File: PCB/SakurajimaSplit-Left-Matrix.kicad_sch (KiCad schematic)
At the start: 42 parts

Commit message: feat(pcb): assign all footprints
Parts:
- D10: renamed from D32; footprint (none) -> Diode_SMD:D_SOD-123
- D11: renamed from D33; footprint (none) -> Diode_SMD:D_SOD-123
- D12: renamed from D34; footprint (none) -> Diode_SMD:D_SOD-123
- D13: renamed from D35; footprint (none) -> Diode_SMD:D_SOD-123
- D14: renamed from D36; footprint (none) -> Diode_SMD:D_SOD-123
- D15: renamed from D37; footprint (none) -> Diode_SMD:D_SOD-123
- D16: renamed from D38; footprint (none) -> Diode_SMD:D_SOD-123
- D17: renamed from D39; footprint (none) -> Diode_SMD:D_SOD-123
- D18: renamed from D40; footprint (none) -> Diode_SMD:D_SOD-123
- D19: renamed from D41; footprint (none) -> Diode_SMD:D_SOD-123
- D20: renamed from D42; footprint (none) -> Diode_SMD:D_SOD-123
- D21: renamed from D43; footprint (none) -> Diode_SMD:D_SOD-123
- D22: renamed from D44; footprint (none) -> Diode_SMD:D_SOD-123
- D23: renamed from D45; footprint (none) -> Diode_SMD:D_SOD-123
- D24: renamed from D46; footprint (none) -> Diode_SMD:D_SOD-123
- D4: renamed from D26; footprint (none) -> Diode_SMD:D_SOD-123
- D5: renamed from D27; footprint (none) -> Diode_SMD:D_SOD-123
- D6: renamed from D28; footprint (none) -> Diode_SMD:D_SOD-123
- D7: renamed from D29; footprint (none) -> Diode_SMD:D_SOD-123
- D8: renamed from D30; footprint (none) -> Diode_SMD:D_SOD-123
- D9: renamed from D31; footprint (none) -> Diode_SMD:D_SOD-123
- MX1: renamed from MX22; footprint (none) -> PCM_marbastlib-mx:SW_MX_1u
- MX10: renamed from MX31; footprint (none) -> PCM_marbastlib-mx:SW_MX_1u
- MX11: renamed from MX32; footprint (none) -> PCM_marbastlib-mx:SW_MX_1u
- MX12: renamed from MX33; footprint (none) -> PCM_marbastlib-mx:SW_MX_1u
- MX13: renamed from MX34; footprint (none) -> PCM_marbastlib-mx:SW_MX_1u
- MX14: renamed from MX35; footprint (none) -> PCM_marbastlib-mx:SW_MX_1u
- MX15: renamed from MX36; footprint (none) -> PCM_marbastlib-mx:SW_MX_1u
- MX16: renamed from MX37; footprint (none) -> PCM_marbastlib-mx:SW_MX_1u
- MX17: renamed from MX38; footprint (none) -> PCM_marbastlib-mx:SW_MX_1u
- MX18: renamed from MX39; footprint (none) -> PCM_marbastlib-mx:SW_MX_1u
- MX19: renamed from MX40; footprint (none) -> PCM_marbastlib-mx:SW_MX_1u
- MX2: renamed from MX23; footprint (none) -> PCM_marbastlib-mx:SW_MX_1u
- MX20: renamed from MX41; footprint (none) -> PCM_marbastlib-mx:SW_MX_1u
- MX21: renamed from MX42; footprint (none) -> PCM_marbastlib-mx:SW_MX_1u
- MX3: renamed from MX24; footprint (none) -> PCM_marbastlib-mx:SW_MX_1u
- MX4: renamed from MX25; footprint (none) -> PCM_marbastlib-mx:SW_MX_1u
- MX5: renamed from MX26; footprint (none) -> PCM_marbastlib-mx:SW_MX_1u
- MX6: renamed from MX27; footprint (none) -> PCM_marbastlib-mx:SW_MX_1u
- MX7: renamed from MX28; footprint (none) -> PCM_marbastlib-mx:SW_MX_1u
- MX8: renamed from MX29; footprint (none) -> PCM_marbastlib-mx:SW_MX_1u
- MX9: renamed from MX30; footprint (none) -> PCM_marbastlib-mx:SW_MX_1u

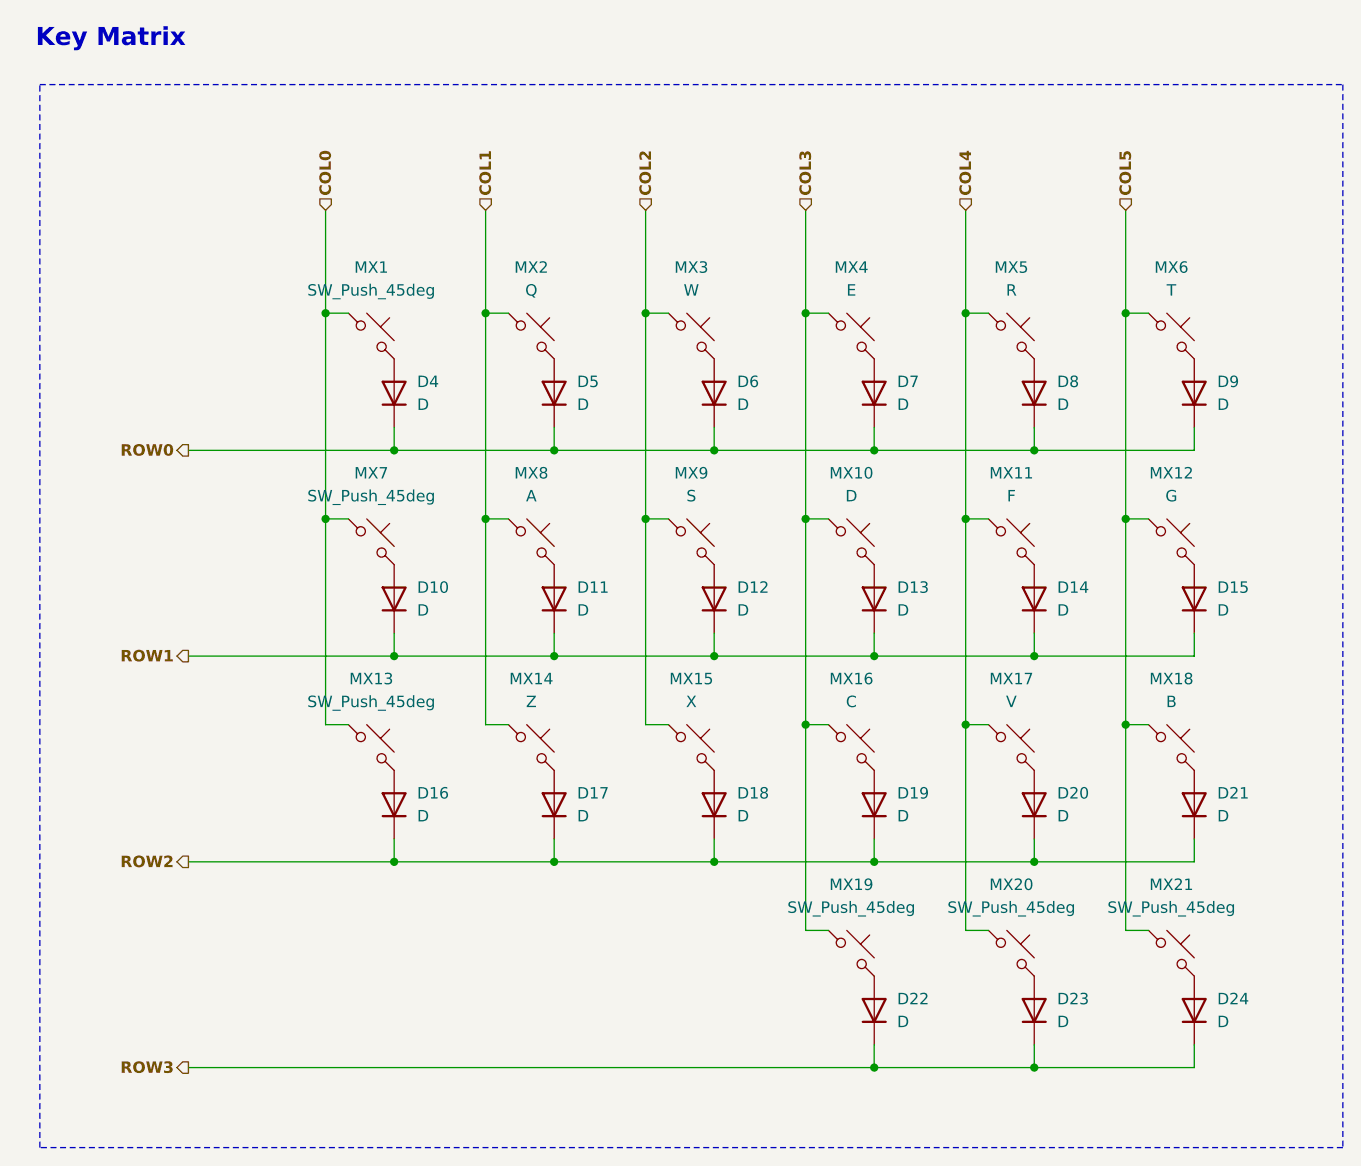
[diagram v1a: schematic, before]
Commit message: fix(sch): fix matrix diode designators not starting from 1
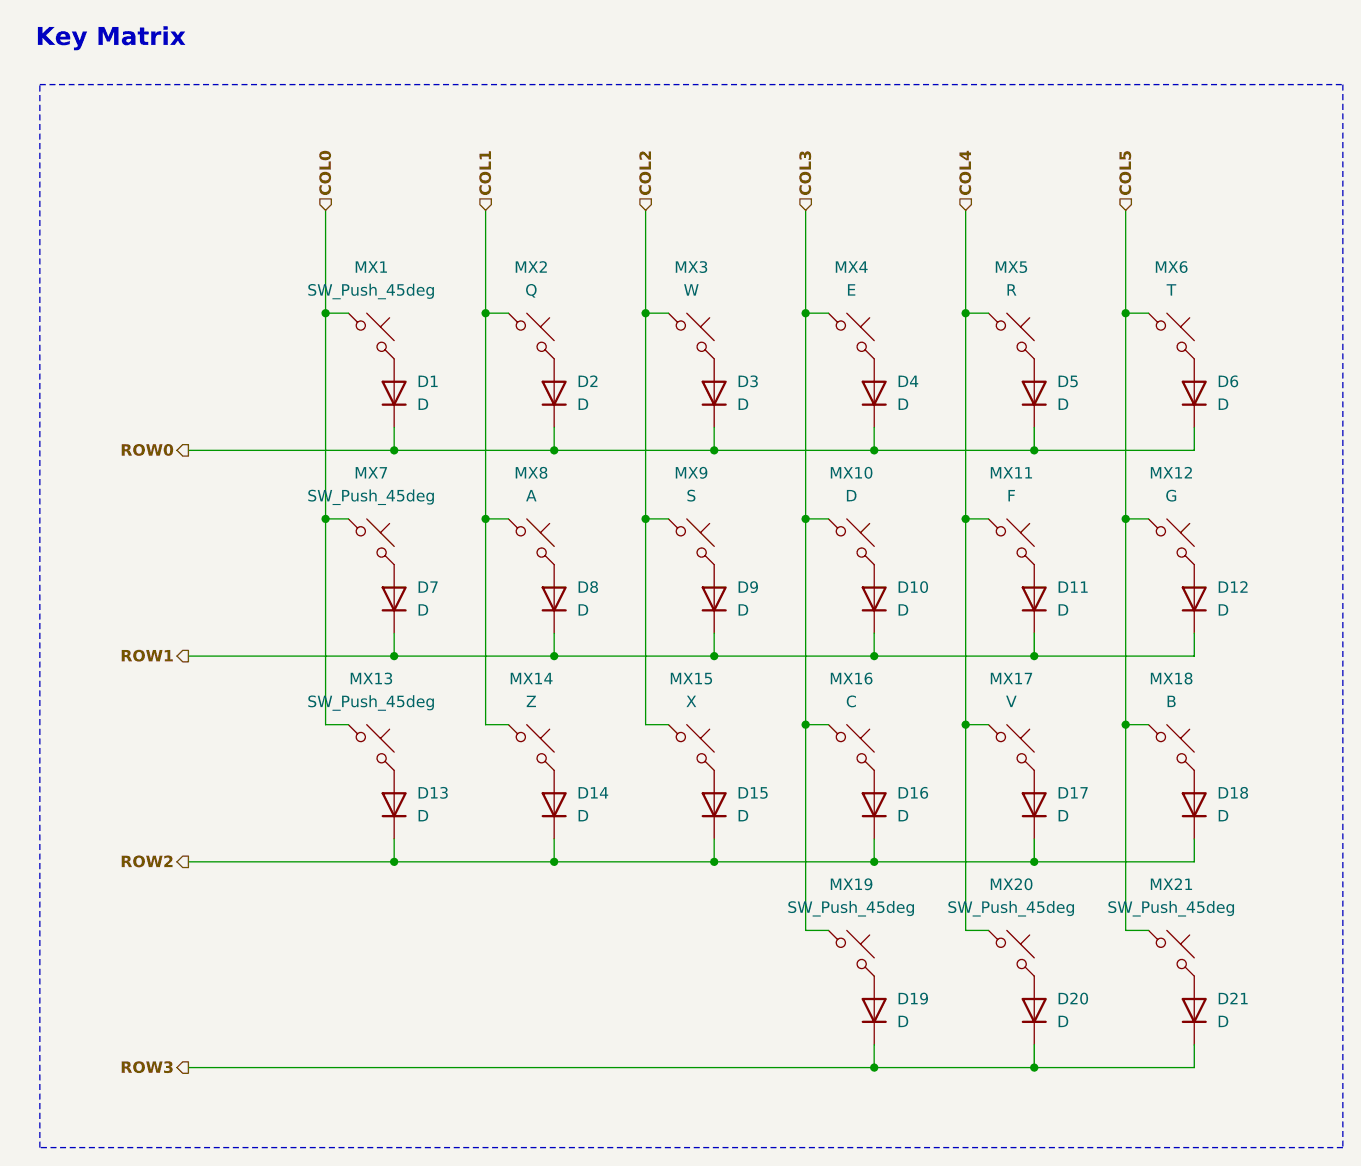
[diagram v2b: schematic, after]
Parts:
- renumbered D4 to D1, D13 to D10, D14 to D11, D15 to D12, D16 to D13, D17 to D14, D18 to D15, D19 to D16, D20 to D17, D21 to D18, D22 to D19, D5 to D2, D23 to D20, D24 to D21, D6 to D3, D7 to D4, D8 to D5, D9 to D6, D10 to D7, D11 to D8, D12 to D9
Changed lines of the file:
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@@
 		(dnp no)
 		(fields_autoplaced yes)
-		(property "Reference" "D21"
+		(property "Reference" "D18"
 			(at 267.97 158.7499 90)
 			(effects
@@
 			(project "SakurajimaSplit"
 				(path "/2049b6de-7453-46e1-ab60-70116abff9d6/d08add9a-e5d5-49be-809e-a90adb11436d/aea2268b-99a7-4c1b-88ca-9db0e6f54310"
-					(reference "D21")
+					(reference "D18")
 					(unit 1)
 				)
@@
 		(dnp no)
 		(fields_autoplaced yes)
-		(property "Reference" "D14"
+		(property "Reference" "D11"
 			(at 250.19 135.8899 90)
 			(effects
@@
 			(project "SakurajimaSplit"
 				(path "/2049b6de-7453-46e1-ab60-70116abff9d6/d08add9a-e5d5-49be-809e-a90adb11436d/aea2268b-99a7-4c1b-88ca-9db0e6f54310"
-					(reference "D14")
+					(reference "D11")
 					(unit 1)
 				)
@@
 		(dnp no)
 		(fields_autoplaced yes)
-		(property "Reference" "D9"
+		(property "Reference" "D6"
 			(at 267.97 113.0299 90)
 			(effects
@@
 			(project "SakurajimaSplit"
 				(path "/2049b6de-7453-46e1-ab60-70116abff9d6/d08add9a-e5d5-49be-809e-a90adb11436d/aea2268b-99a7-4c1b-88ca-9db0e6f54310"
-					(reference "D9")
+					(reference "D6")
 					(unit 1)
 				)
@@
 		(dnp no)
 		(fields_autoplaced yes)
-		(property "Reference" "D5"
+		(property "Reference" "D2"
 			(at 196.85 113.0299 90)
 			(effects
@@
 			(project "SakurajimaSplit"
 				(path "/2049b6de-7453-46e1-ab60-70116abff9d6/d08add9a-e5d5-49be-809e-a90adb11436d/aea2268b-99a7-4c1b-88ca-9db0e6f54310"
-					(reference "D5")
+					(reference "D2")
 					(unit 1)
 				)
@@
 		(dnp no)
 		(fields_autoplaced yes)
-		(property "Reference" "D12"
+		(property "Reference" "D9"
 			(at 214.63 135.8899 90)
 			(effects
@@
 			(project "SakurajimaSplit"
 				(path "/2049b6de-7453-46e1-ab60-70116abff9d6/d08add9a-e5d5-49be-809e-a90adb11436d/aea2268b-99a7-4c1b-88ca-9db0e6f54310"
-					(reference "D12")
+					(reference "D9")
 					(unit 1)
 				)
@@
 		(dnp no)
 		(fields_autoplaced yes)
-		(property "Reference" "D13"
+		(property "Reference" "D10"
 			(at 232.41 135.8899 90)
 			(effects
@@
 			(project "SakurajimaSplit"
 				(path "/2049b6de-7453-46e1-ab60-70116abff9d6/d08add9a-e5d5-49be-809e-a90adb11436d/aea2268b-99a7-4c1b-88ca-9db0e6f54310"
-					(reference "D13")
+					(reference "D10")
 					(unit 1)
 				)
@@
 		(dnp no)
 		(fields_autoplaced yes)
-		(property "Reference" "D24"
+		(property "Reference" "D21"
 			(at 267.97 181.6099 90)
 			(effects
@@
 			(project "SakurajimaSplit"
 				(path "/2049b6de-7453-46e1-ab60-70116abff9d6/d08add9a-e5d5-49be-809e-a90adb11436d/aea2268b-99a7-4c1b-88ca-9db0e6f54310"
-					(reference "D24")
+					(reference "D21")
 					(unit 1)
 				)
@@
 		(dnp no)
 		(fields_autoplaced yes)
-		(property "Reference" "D6"
+		(property "Reference" "D3"
 			(at 214.63 113.0299 90)
 			(effects
@@
 			(project "SakurajimaSplit"
 				(path "/2049b6de-7453-46e1-ab60-70116abff9d6/d08add9a-e5d5-49be-809e-a90adb11436d/aea2268b-99a7-4c1b-88ca-9db0e6f54310"
-					(reference "D6")
+					(reference "D3")
 					(unit 1)
 				)
@@
 		(dnp no)
 		(fields_autoplaced yes)
-		(property "Reference" "D18"
+		(property "Reference" "D15"
 			(at 214.63 158.7499 90)
 			(effects
@@
 			(project "SakurajimaSplit"
 				(path "/2049b6de-7453-46e1-ab60-70116abff9d6/d08add9a-e5d5-49be-809e-a90adb11436d/aea2268b-99a7-4c1b-88ca-9db0e6f54310"
-					(reference "D18")
+					(reference "D15")
 					(unit 1)
 				)
@@
 		(dnp no)
 		(fields_autoplaced yes)
-		(property "Reference" "D16"
+		(property "Reference" "D13"
 			(at 179.07 158.7499 90)
 			(effects
@@
 			(project "SakurajimaSplit"
 				(path "/2049b6de-7453-46e1-ab60-70116abff9d6/d08add9a-e5d5-49be-809e-a90adb11436d/aea2268b-99a7-4c1b-88ca-9db0e6f54310"
-					(reference "D16")
+					(reference "D13")
 					(unit 1)
 				)
@@
 		(dnp no)
 		(fields_autoplaced yes)
-		(property "Reference" "D10"
+		(property "Reference" "D7"
 			(at 179.07 135.8899 90)
 			(effects
@@
 			(project "SakurajimaSplit"
 				(path "/2049b6de-7453-46e1-ab60-70116abff9d6/d08add9a-e5d5-49be-809e-a90adb11436d/aea2268b-99a7-4c1b-88ca-9db0e6f54310"
-					(reference "D10")
+					(reference "D7")
 					(unit 1)
 				)
@@
 		(dnp no)
 		(fields_autoplaced yes)
-		(property "Reference" "D11"
+		(property "Reference" "D8"
 			(at 196.85 135.8899 90)
 			(effects
@@
 			(project "SakurajimaSplit"
 				(path "/2049b6de-7453-46e1-ab60-70116abff9d6/d08add9a-e5d5-49be-809e-a90adb11436d/aea2268b-99a7-4c1b-88ca-9db0e6f54310"
-					(reference "D11")
+					(reference "D8")
 					(unit 1)
 				)
@@
 		(dnp no)
 		(fields_autoplaced yes)
-		(property "Reference" "D15"
+		(property "Reference" "D12"
 			(at 267.97 135.8899 90)
 			(effects
@@
 			(project "SakurajimaSplit"
 				(path "/2049b6de-7453-46e1-ab60-70116abff9d6/d08add9a-e5d5-49be-809e-a90adb11436d/aea2268b-99a7-4c1b-88ca-9db0e6f54310"
-					(reference "D15")
+					(reference "D12")
 					(unit 1)
 				)
@@
 		(dnp no)
 		(fields_autoplaced yes)
-		(property "Reference" "D17"
+		(property "Reference" "D14"
 			(at 196.85 158.7499 90)
 			(effects
@@
 			(project "SakurajimaSplit"
 				(path "/2049b6de-7453-46e1-ab60-70116abff9d6/d08add9a-e5d5-49be-809e-a90adb11436d/aea2268b-99a7-4c1b-88ca-9db0e6f54310"
-					(reference "D17")
+					(reference "D14")
 					(unit 1)
 				)
@@
 		(dnp no)
 		(fields_autoplaced yes)
-		(property "Reference" "D19"
+		(property "Reference" "D16"
 			(at 232.41 158.7499 90)
 			(effects
@@
 			(project "SakurajimaSplit"
 				(path "/2049b6de-7453-46e1-ab60-70116abff9d6/d08add9a-e5d5-49be-809e-a90adb11436d/aea2268b-99a7-4c1b-88ca-9db0e6f54310"
-					(reference "D19")
+					(reference "D16")
 					(unit 1)
 				)
@@
 		(dnp no)
 		(fields_autoplaced yes)
-		(property "Reference" "D7"
+		(property "Reference" "D4"
 			(at 232.41 113.0299 90)
 			(effects
@@
 			(project "SakurajimaSplit"
 				(path "/2049b6de-7453-46e1-ab60-70116abff9d6/d08add9a-e5d5-49be-809e-a90adb11436d/aea2268b-99a7-4c1b-88ca-9db0e6f54310"
-					(reference "D7")
+					(reference "D4")
 					(unit 1)
 				)
@@
 		(dnp no)
 		(fields_autoplaced yes)
-		(property "Reference" "D22"
+		(property "Reference" "D19"
 			(at 232.41 181.6099 90)
 			(effects
@@
 			(project "SakurajimaSplit"
 				(path "/2049b6de-7453-46e1-ab60-70116abff9d6/d08add9a-e5d5-49be-809e-a90adb11436d/aea2268b-99a7-4c1b-88ca-9db0e6f54310"
-					(reference "D22")
+					(reference "D19")
 					(unit 1)
 				)
@@
 		(dnp no)
 		(fields_autoplaced yes)
-		(property "Reference" "D23"
+		(property "Reference" "D20"
 			(at 250.19 181.6099 90)
 			(effects
@@
 			(project "SakurajimaSplit"
 				(path "/2049b6de-7453-46e1-ab60-70116abff9d6/d08add9a-e5d5-49be-809e-a90adb11436d/aea2268b-99a7-4c1b-88ca-9db0e6f54310"
-					(reference "D23")
+					(reference "D20")
 					(unit 1)
 				)
@@
 		(dnp no)
 		(fields_autoplaced yes)
-		(property "Reference" "D20"
+		(property "Reference" "D17"
 			(at 250.19 158.7499 90)
 			(effects
@@
 			(project "SakurajimaSplit"
 				(path "/2049b6de-7453-46e1-ab60-70116abff9d6/d08add9a-e5d5-49be-809e-a90adb11436d/aea2268b-99a7-4c1b-88ca-9db0e6f54310"
-					(reference "D20")
+					(reference "D17")
 					(unit 1)
 				)
@@
 		(dnp no)
 		(fields_autoplaced yes)
-		(property "Reference" "D8"
+		(property "Reference" "D5"
 			(at 250.19 113.0299 90)
 			(effects
@@
 			(project "SakurajimaSplit"
 				(path "/2049b6de-7453-46e1-ab60-70116abff9d6/d08add9a-e5d5-49be-809e-a90adb11436d/aea2268b-99a7-4c1b-88ca-9db0e6f54310"
-					(reference "D8")
+					(reference "D5")
 					(unit 1)
 				)
@@
 		(dnp no)
 		(fields_autoplaced yes)
-		(property "Reference" "D4"
+		(property "Reference" "D1"
 			(at 179.07 113.0299 90)
 			(effects
@@
 			(project "SakurajimaSplit"
 				(path "/2049b6de-7453-46e1-ab60-70116abff9d6/d08add9a-e5d5-49be-809e-a90adb11436d/aea2268b-99a7-4c1b-88ca-9db0e6f54310"
-					(reference "D4")
+					(reference "D1")
 					(unit 1)
 				)

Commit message: fix(sch): fix wrong footprint for MX21 & MX40
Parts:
- MX21: footprint PCM_marbastlib-mx:SW_MX_1u -> PCM_marbastlib-mx:SW_MX_1.5u
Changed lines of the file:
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@@
 			)
 		)
-		(property "Footprint" "PCM_marbastlib-mx:SW_MX_1u"
+		(property "Footprint" "PCM_marbastlib-mx:SW_MX_1.5u"
 			(at 262.89 176.53 0)
 			(effects
